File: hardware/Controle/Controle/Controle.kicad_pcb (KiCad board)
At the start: 2 copper layers, 70 x 35.8 mm, 82 parts, among them J101 USART, J102 ST_LINK, J103 FAN, J105 Iin_sen, J106 Iin_sen, J107 Driver-Sense, J301 RJ45, Q101 BCV27, U201 MCP2561-E-SN, U401 AMS1117-3.3, U402 AMS1117-5, U403 K78L15-1000R3, U501 STM32G431CBT6, U601 TL7726IDR

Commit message: export files
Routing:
- net GND: vias 69 -> 68
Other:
- rule via_min_size: 0.4 -> 0.45

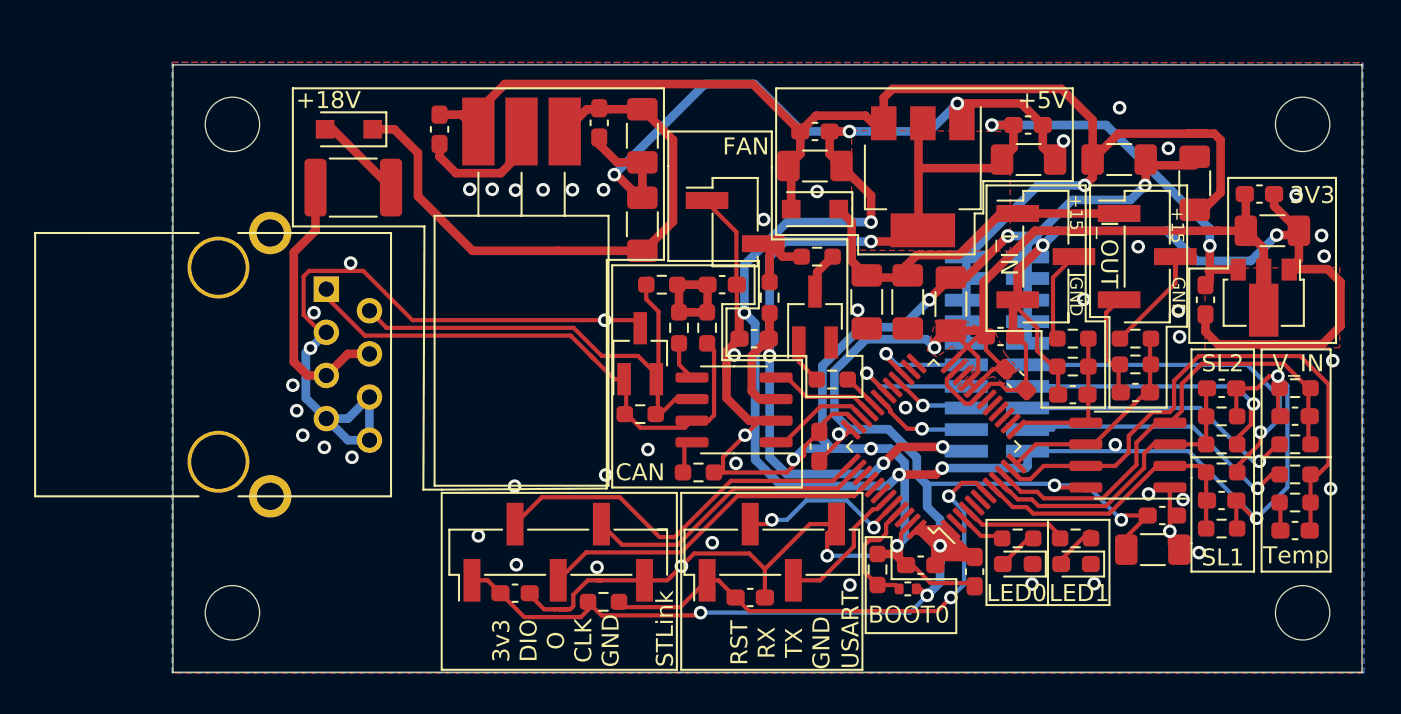
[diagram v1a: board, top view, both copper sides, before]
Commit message: dimensions and holes modified
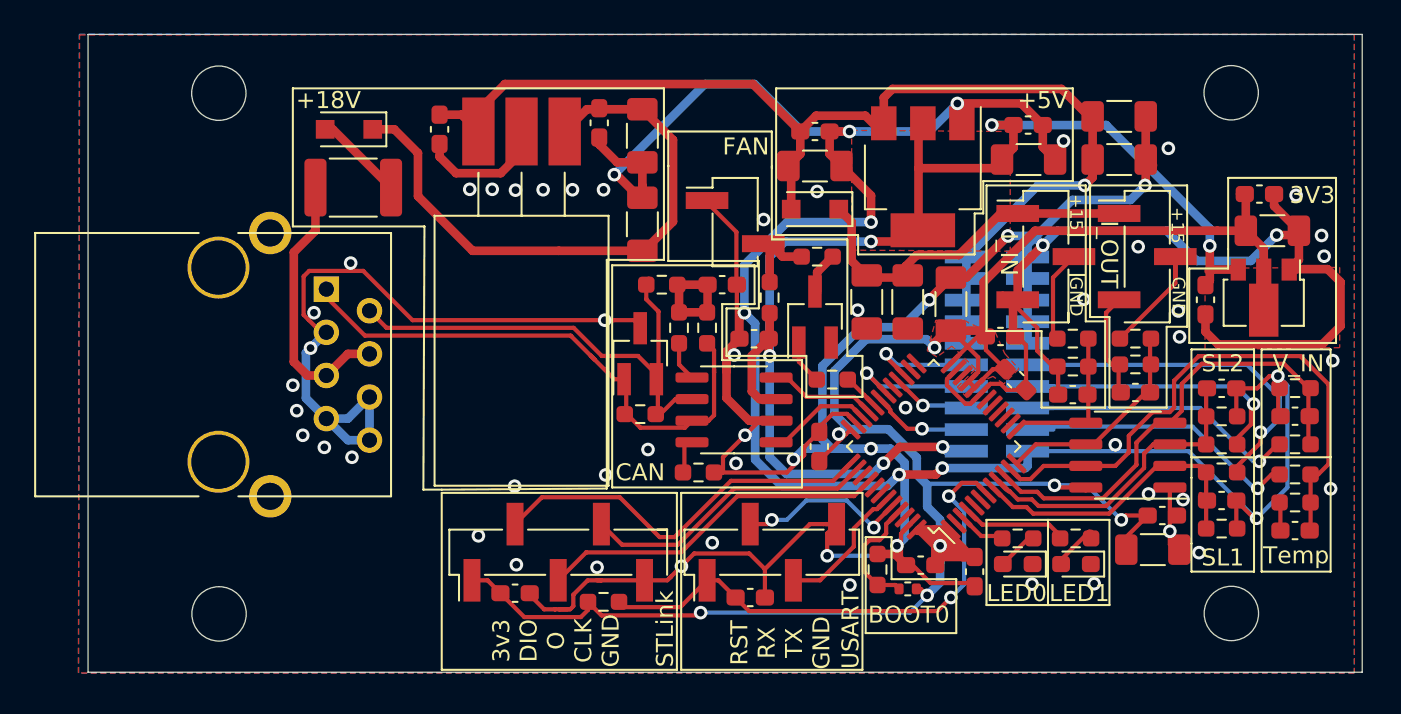
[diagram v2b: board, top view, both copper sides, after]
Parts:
- C605, C606: value ? -> NC
- moved H101 30.6 mm to (128.4, 55.1), turned to 180 degrees
- moved H102 28.8 mm to (128.4, 85.8), turned to 180 degrees
- moved C1 5.94 mm to (181.4, 56.5), turned to 180 degrees
- moved H104 4.60 mm to (188.0, 55.1)
- moved H103 4.20 mm to (188.0, 85.8)
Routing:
- net +15V: track 83.4 -> 69.0 mm
- net GND: track 372.2 -> 372.3 mm, vias 68 -> 67
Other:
- board size 70 x 35.8 mm -> 75 x 37.5 mm

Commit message: dimensions reduced
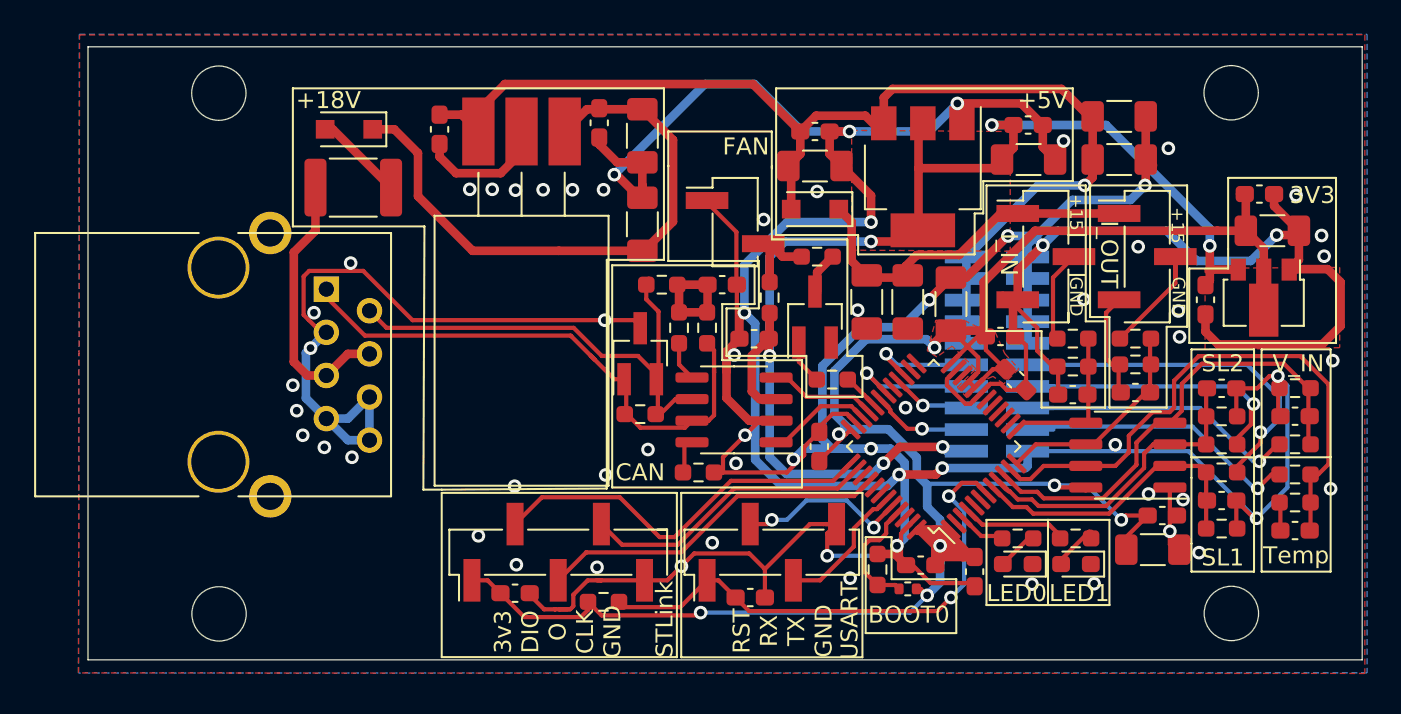
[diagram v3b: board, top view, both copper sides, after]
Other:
- board size 75 x 37.5 mm -> 75 x 36.1 mm
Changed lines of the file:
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@@
   (page A4)
   (layers
-    (0 F.Cu signal hide)
+    (0 F.Cu signal)
     (31 B.Cu signal)
     (32 B.Adhes user)
@@
     (38 B.Mask user)
     (39 F.Mask user)
-    (40 Dwgs.User user hide)
+    (40 Dwgs.User user)
     (41 Cmts.User user)
     (42 Eco1.User user)
@@
     )
   )
-  (dimension 18.76298 (width 0.15) (layer Dwgs.User)
-    (gr_text "18.763 mm" (at 212.312 61.11883 90) (layer Dwgs.User)
+  (dimension 18.08598 (width 0.15) (layer Dwgs.User)
+    (gr_text "18.086 mm" (at 233.81206 61.457243 89.99961984) (layer Dwgs.User)
       (effects (font (size 1 1) (thickness 0.15)))
     )
-    (feature1 (pts (xy 174.22628 51.73734) (xy 211.598421 51.73734)))
-    (feature2 (pts (xy 174.22628 70.50032) (xy 211.598421 70.50032)))
-    (crossbar (pts (xy 211.012 70.50032) (xy 211.012 51.73734)))
-    (arrow1a (pts (xy 211.012 51.73734) (xy 211.598421 52.863844)))
-    (arrow1b (pts (xy 211.012 51.73734) (xy 210.425579 52.863844)))
-    (arrow2a (pts (xy 211.012 70.50032) (xy 211.598421 69.373816)))
-    (arrow2b (pts (xy 211.012 70.50032) (xy 210.425579 69.373816)))
-  )
-  (dimension 18.77568 (width 0.15) (layer Dwgs.User)
-    (gr_text "18.776 mm" (at 212.439 79.88816 270) (layer Dwgs.User)
-      (effects (font (size 1 1) (thickness 0.15)))
-    )
-    (feature1 (pts (xy 174.22628 89.276) (xy 211.725421 89.276)))
-    (feature2 (pts (xy 174.22628 70.50032) (xy 211.725421 70.50032)))
-    (crossbar (pts (xy 211.139 70.50032) (xy 211.139 89.276)))
-    (arrow1a (pts (xy 211.139 89.276) (xy 210.552579 88.149496)))
-    (arrow1b (pts (xy 211.139 89.276) (xy 211.725421 88.149496)))
-    (arrow2a (pts (xy 211.139 70.50032) (xy 210.552579 71.626824)))
-    (arrow2b (pts (xy 211.139 70.50032) (xy 211.725421 71.626824)))
-  )
-  (gr_line (start 195.7264 89.22934) (end 120.72292 89.22998) (layer Edge.Cuts) (width 0.05))
-  (gr_line (start 195.7264 51.684) (end 195.7264 89.22934) (layer Edge.Cuts) (width 0.05))
-  (gr_line (start 120.72292 51.684) (end 195.7264 51.684) (layer Edge.Cuts) (width 0.05))
-  (gr_line (start 120.72292 89.22998) (end 120.72292 51.684) (layer Edge.Cuts) (width 0.05))
+    (feature1 (pts (xy 195.7264 52.414) (xy 233.098541 52.414248)))
+    (feature2 (pts (xy 195.72628 70.49998) (xy 233.098421 70.500228)))
+    (crossbar (pts (xy 232.512 70.500224) (xy 232.51212 52.414244)))
+    (arrow1a (pts (xy 232.51212 52.414244) (xy 233.098533 53.540752)))
+    (arrow1b (pts (xy 232.51212 52.414244) (xy 231.925692 53.540744)))
+    (arrow2a (pts (xy 232.512 70.500224) (xy 233.098428 69.373724)))
+    (arrow2b (pts (xy 232.512 70.500224) (xy 231.925587 69.373716)))
+  )
+  (dimension 17.999 (width 0.15) (layer Dwgs.User)
+    (gr_text "17.999 mm" (at 233.93906 79.499225 270.000382) (layer Dwgs.User)
+      (effects (font (size 1 1) (thickness 0.15)))
+    )
+    (feature1 (pts (xy 195.7264 88.49898) (xy 233.225541 88.49873)))
+    (feature2 (pts (xy 195.72628 70.49998) (xy 233.225421 70.49973)))
+    (crossbar (pts (xy 232.639 70.499734) (xy 232.63912 88.498734)))
+    (arrow1a (pts (xy 232.63912 88.498734) (xy 232.052692 87.372234)))
+    (arrow1b (pts (xy 232.63912 88.498734) (xy 233.225533 87.372226)))
+    (arrow2a (pts (xy 232.639 70.499734) (xy 232.052587 71.626242)))
+    (arrow2b (pts (xy 232.639 70.499734) (xy 233.225428 71.626234)))
+  )
+  (gr_line (start 195.7264 88.49934) (end 120.72292 88.49998) (layer Edge.Cuts) (width 0.05))
+  (gr_line (start 195.7264 52.414) (end 195.7264 88.49898) (layer Edge.Cuts) (width 0.05))
+  (gr_line (start 120.72292 52.414) (end 195.7264 52.414) (layer Edge.Cuts) (width 0.05))
+  (gr_line (start 120.72292 88.49998) (end 120.72292 52.414) (layer Edge.Cuts) (width 0.05))
   (gr_text +15 (at 184.85 62.9235 -90) (layer F.SilkS)
     (effects (font (size 0.746 0.746) (thickness 0.15)))
@@
   )
   (gr_line (start 166.308 78.6715) (end 155.64 78.6715) (layer F.SilkS) (width 0.12))
-  (gr_line (start 166.308 89.0855) (end 166.308 78.6715) (layer F.SilkS) (width 0.12))
-  (gr_line (start 155.64 89.0855) (end 166.308 89.0855) (layer F.SilkS) (width 0.12))
-  (gr_line (start 155.64 78.6715) (end 155.64 89.0855) (layer F.SilkS) (width 0.12))
-  (gr_text USART (at 165.6095 86.736 90) (layer F.SilkS)
+  (gr_line (start 166.308 88.34998) (end 166.308 78.6715) (layer F.SilkS) (width 0.12))
+  (gr_line (start 155.64292 88.34998) (end 166.30292 88.34998) (layer F.SilkS) (width 0.12))
+  (gr_line (start 155.64 78.6715) (end 155.64 88.34998) (layer F.SilkS) (width 0.12))
+  (gr_text USART (at 165.55292 86.18998 90) (layer F.SilkS)
     (effects (font (size 1 1) (thickness 0.15)))
   )
-  (gr_text STLink (at 154.6875 86.6725 90) (layer F.SilkS)
+  (gr_text STLink (at 154.66292 86.09998 90) (layer F.SilkS)
     (effects (font (size 1 1) (thickness 0.15)))
   )
   (gr_line (start 155.386 78.6715) (end 141.543 78.6715) (layer F.SilkS) (width 0.12))
-  (gr_line (start 155.386 89.0855) (end 155.386 78.6715) (layer F.SilkS) (width 0.12))
-  (gr_line (start 141.543 89.0855) (end 155.386 89.0855) (layer F.SilkS) (width 0.12))
-  (gr_line (start 141.543 78.6715) (end 141.543 89.0855) (layer F.SilkS) (width 0.12))
-  (gr_text "3v3\nDIO\nO\nCLK\nGND" (at 148.274 87.371 90) (layer F.SilkS)
+  (gr_line (start 155.386 88.34998) (end 155.386 78.6715) (layer F.SilkS) (width 0.12))
+  (gr_line (start 141.543 88.33998) (end 155.386 88.33998) (layer F.SilkS) (width 0.12))
+  (gr_line (start 141.543 78.6715) (end 141.543 88.33998) (layer F.SilkS) (width 0.12))
+  (gr_text "3v3\nDIO\nO\nCLK\nGND" (at 148.37292 86.84998 90) (layer F.SilkS)
     (effects (font (size 1 1) (thickness 0.15)))
   )
-  (gr_text "RST\nRX\nTX\nGND" (at 161.482 87.498 90) (layer F.SilkS)
+  (gr_text "RST\nRX\nTX\nGND" (at 161.61292 86.79998 90) (layer F.SilkS)
     (effects (font (size 1 1) (thickness 0.15)))
   )
@@
   (gr_line (start 151.576 78.354) (end 162.752 78.354) (layer F.SilkS) (width 0.12))
   (gr_line (start 151.576 65.273) (end 151.576 78.354) (layer F.SilkS) (width 0.12))
-  (dimension 75 (width 0.15) (layer Dwgs.User)
-    (gr_text "75.000 mm" (at 158.22292 94.816981) (layer Dwgs.User)
+  (dimension 74.993481 (width 0.15) (layer Dwgs.User)
+    (gr_text "74.993 mm" (at 158.230472 94.041481 0.008404111532) (layer Dwgs.User)
       (effects (font (size 1 1) (thickness 0.15)))
     )
-    (feature1 (pts (xy 195.72292 89.27998) (xy 195.72292 94.103402)))
-    (feature2 (pts (xy 120.72292 89.27998) (xy 120.72292 94.103402)))
-    (crossbar (pts (xy 120.72292 93.516981) (xy 195.72292 93.516981)))
-    (arrow1a (pts (xy 195.72292 93.516981) (xy 194.596416 94.103402)))
-    (arrow1b (pts (xy 195.72292 93.516981) (xy 194.596416 92.93056)))
-    (arrow2a (pts (xy 120.72292 93.516981) (xy 121.849424 94.103402)))
-    (arrow2b (pts (xy 120.72292 93.516981) (xy 121.849424 92.93056)))
-  )
-  (dimension 39.624034 (width 0.15) (layer Dwgs.User)
-    (gr_text "39.624 mm" (at 206.062991 71.482461 270.0751913) (layer Dwgs.User)
-      (effects (font (size 1 1) (thickness 0.15)))
-    )
-    (feature1 (pts (xy 195.772 91.308) (xy 205.375412 91.295397)))
-    (feature2 (pts (xy 195.72 51.684) (xy 205.323412 51.671397)))
-    (crossbar (pts (xy 204.736992 51.672167) (xy 204.788992 91.296167)))
-    (arrow1a (pts (xy 204.788992 91.296167) (xy 204.201093 90.170434)))
-    (arrow1b (pts (xy 204.788992 91.296167) (xy 205.373934 90.168895)))
-    (arrow2a (pts (xy 204.736992 51.672167) (xy 204.15205 52.799439)))
-    (arrow2b (pts (xy 204.736992 51.672167) (xy 205.324891 52.7979)))
+    (feature1 (pts (xy 195.7264 88.49898) (xy 195.727107 93.322402)))
+    (feature2 (pts (xy 120.73292 88.50998) (xy 120.733627 93.333402)))
+    (crossbar (pts (xy 120.733541 92.746981) (xy 195.727021 92.735981)))
+    (arrow1a (pts (xy 195.727021 92.735981) (xy 194.600603 93.322567)))
+    (arrow1b (pts (xy 195.727021 92.735981) (xy 194.600431 92.149726)))
+    (arrow2a (pts (xy 120.733541 92.746981) (xy 121.860131 93.333236)))
+    (arrow2b (pts (xy 120.733541 92.746981) (xy 121.859959 92.160395)))
+  )
+  (dimension 36.08534 (width 0.15) (layer Dwgs.User)
+    (gr_text "36.085 mm" (at 206.0434 70.45667 270) (layer Dwgs.User)
+      (effects (font (size 1 1) (thickness 0.15)))
+    )
+    (feature1 (pts (xy 195.7264 88.49934) (xy 205.329821 88.49934)))
+    (feature2 (pts (xy 195.7264 52.414) (xy 205.329821 52.414)))
+    (crossbar (pts (xy 204.7434 52.414) (xy 204.7434 88.49934)))
+    (arrow1a (pts (xy 204.7434 88.49934) (xy 204.156979 87.372836)))
+    (arrow1b (pts (xy 204.7434 88.49934) (xy 205.329821 87.372836)))
+    (arrow2a (pts (xy 204.7434 52.414) (xy 204.156979 53.540504)))
+    (arrow2b (pts (xy 204.7434 52.414) (xy 205.329821 53.540504)))
   )
   (dimension 21.5 (width 0.15) (layer Dwgs.User)
@@
   (segment (start 190.66194 71.79614) (end 190.76354 71.79614) (width 0.508) (layer B.Cu) (net 2))
   (segment (start 190.26486 71.79614) (end 190.76354 71.79614) (width 0.25) (layer F.Cu) (net 2))
-  (via (at 165.5714 84.0944) (size 0.8) (drill 0.45) (layers F.Cu B.Cu) (net 2))
+  (via (at 165.58292 83.68998) (size 0.8) (drill 0.45) (layers F.Cu B.Cu) (net 2))
   (via (at 166.0286 67.9146) (size 0.8) (drill 0.45) (layers F.Cu B.Cu) (net 2))
   (via (at 178.1444 57.9578) (size 0.8) (drill 0.45) (layers F.Cu B.Cu) (net 2))
@@
     (polygon
       (pts
-        (xy 195.26292 51.69035) (xy 195.26292 89.276) (xy 120.16292 89.276) (xy 120.21292 51.67765)
+        (xy 196.01292 51.677211) (xy 196.01292 89.26275) (xy 120.16292 89.276) (xy 120.21292 51.67765)
       )
     )
@@
     (polygon
       (pts
-        (xy 195.26292 51.66998) (xy 195.26292 89.26998) (xy 120.16292 89.26998) (xy 120.226807 51.716662)
+        (xy 195.88292 51.699804) (xy 195.88292 89.300157) (xy 120.16292 89.26998) (xy 120.226807 51.716662)
       )
     )

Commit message: Gerbers re-generated with JCLJCLJLC.. string
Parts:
- added REF**: OSHW-Logo2_7.3x6mm_SilkScreen, Symbol:OSHW-Logo2_7.3x6mm_SilkScreen, F.Cu at (137.0, 83.5)
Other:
- board text added: "JLCJLCJLCJLC"
